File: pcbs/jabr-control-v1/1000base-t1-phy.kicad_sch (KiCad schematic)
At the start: 17 parts, among them U8001 LAN8870, Y8001 XRCGB25M000F3A16R0

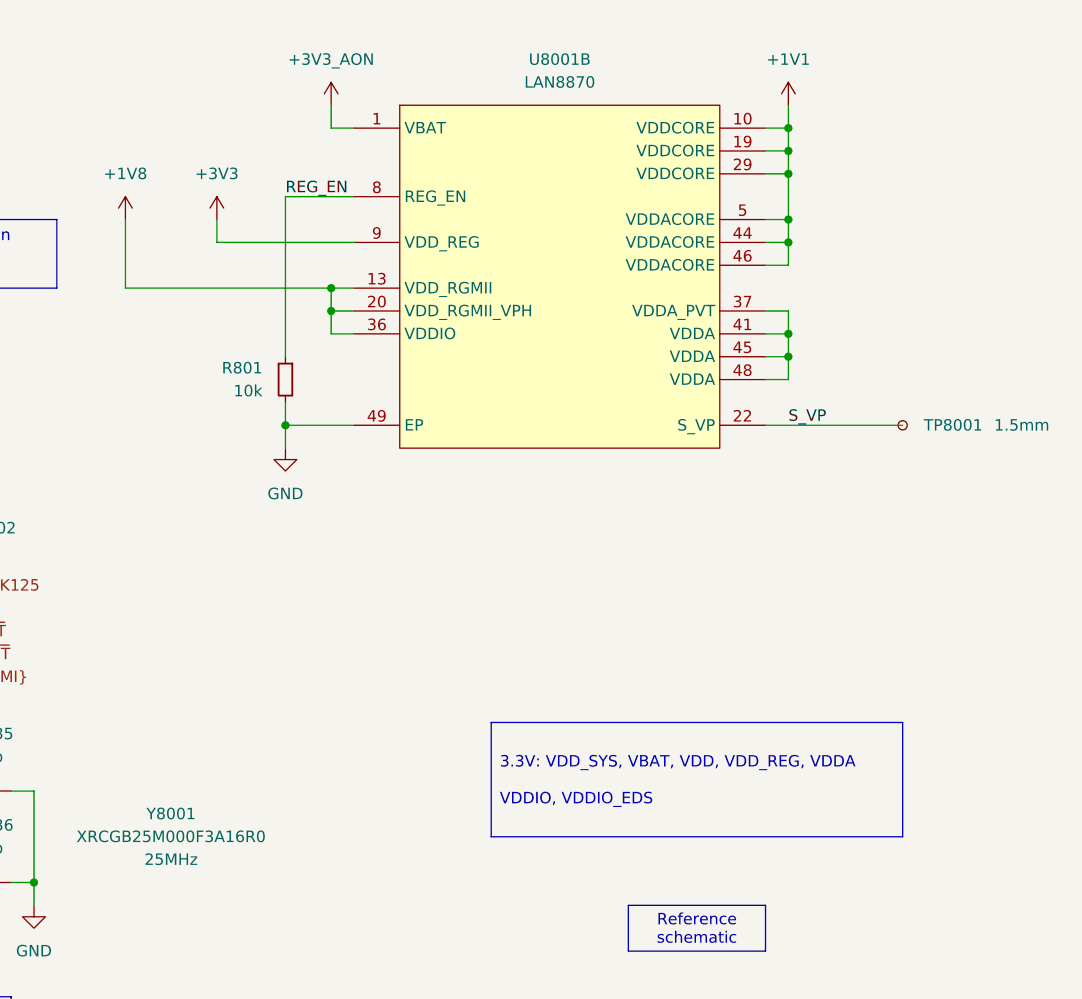
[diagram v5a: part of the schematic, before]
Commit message: Schematic nearing completion, need to do GPIO and PHY decouplings caps
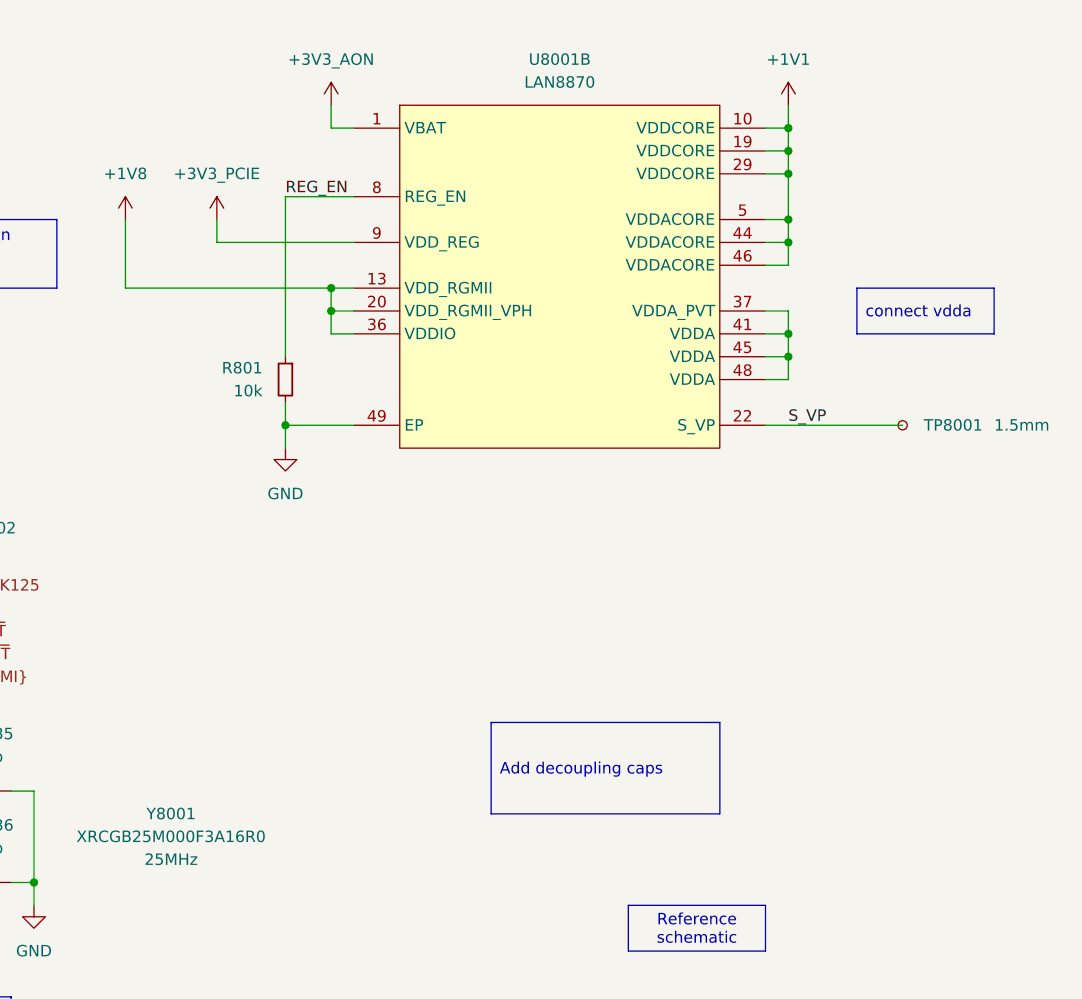
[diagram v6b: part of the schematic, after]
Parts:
- TP8001, TP8002, TP801: footprint TestPoint:TestPoint_Pad_D1.5mm -> project_footprints:TestPoint_Pad_D1.5mm; now left out of the parts list
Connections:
- net +3V3 renamed +3V3_PCIE
